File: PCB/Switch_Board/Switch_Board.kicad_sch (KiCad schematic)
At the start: 5 parts

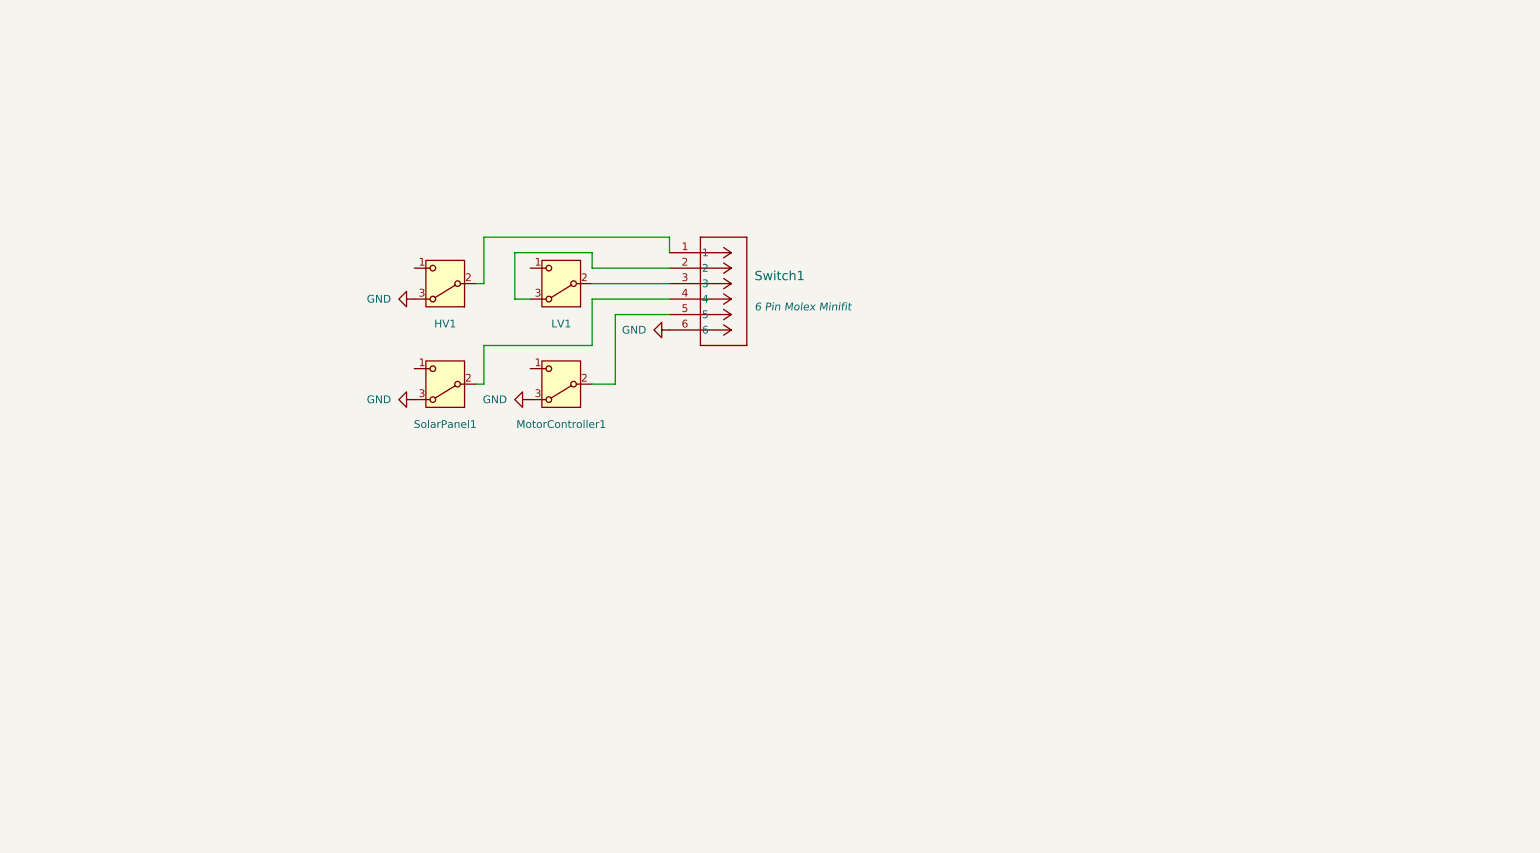
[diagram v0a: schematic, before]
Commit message: Change pinout to match BMS
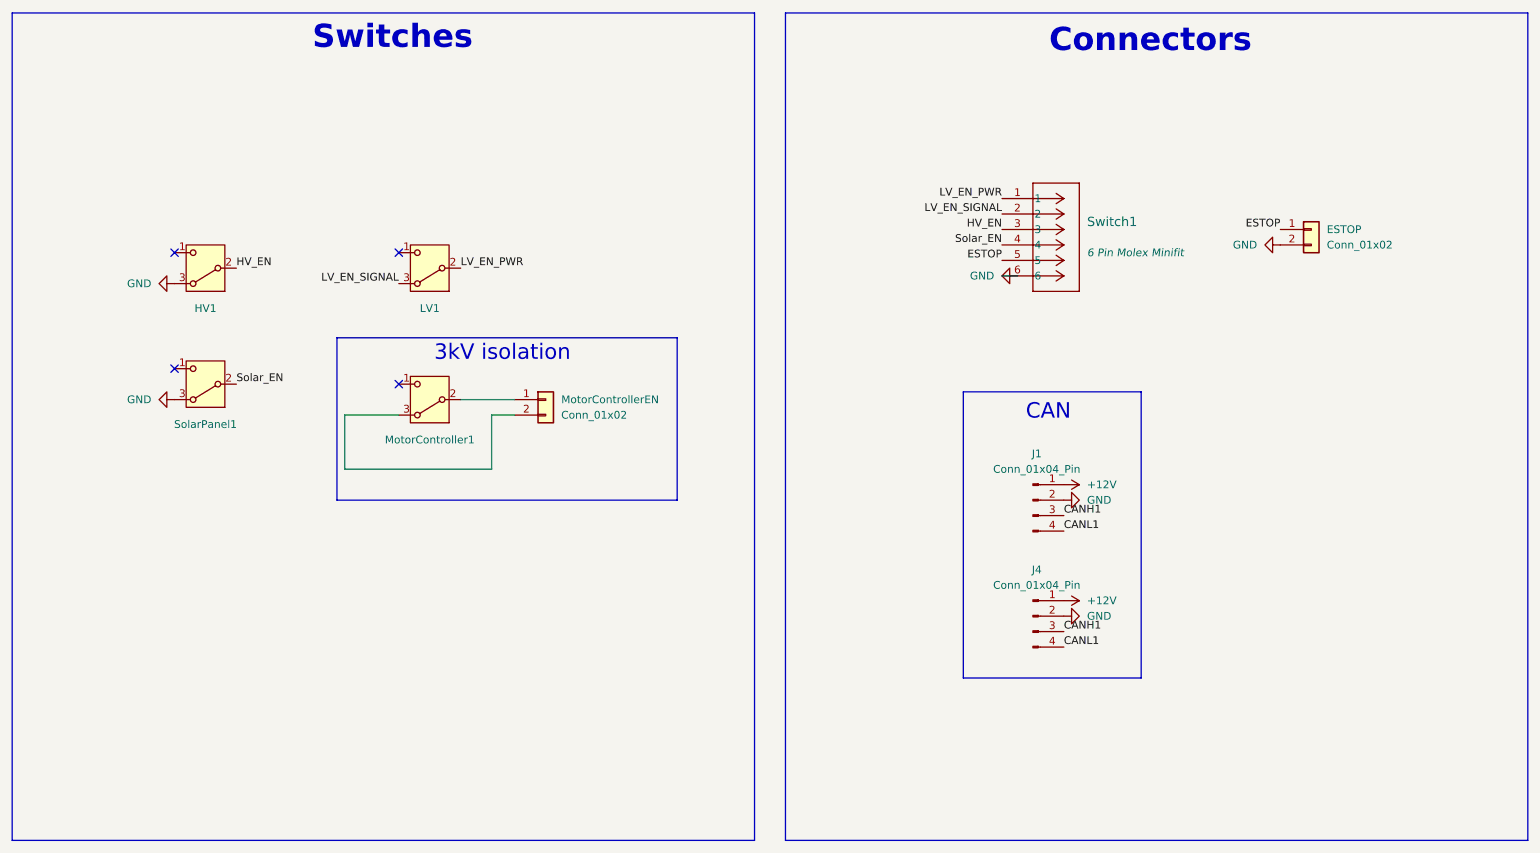
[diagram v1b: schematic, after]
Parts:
- added ESTOP, MotorControllerEN: Conn_01x02, Connector_Molex:Molex_Mini-Fit_Jr_5569-02A2_2x01_P4.20mm_Horizontal, symbol Connector_Generic:Conn_01x02
- added J1, J4: Conn_01x04_Pin, Connector_Molex:Molex_Mini-Fit_Jr_5569-04A2_2x02_P4.20mm_Horizontal, symbol Connector:Conn_01x04_Pin
- Switch1: value ~ -> (none)
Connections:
- net GND: now also ESTOP.2 (Pin_2), J1.2 (Pin_2), J4.2 (Pin_2); no longer MotorController1.3 (A)
- net Solar_EN: now reaches SolarPanel1.2 (B), Switch1.4
- net HV_EN: now reaches HV1.2 (B)
- net HV_EN: now also Switch1.3; no longer Switch1.1
- net LV_EN_PWR: now reaches LV1.2 (B)
- net LV_EN_PWR: now also Switch1.1; no longer Switch1.3
- net LV_EN_SIGNAL: now reaches LV1.3 (A), Switch1.2
- net at MotorController1.2 (B): now also MotorControllerEN.1 (Pin_1); no longer Switch1.5
- new net: MotorController1.3 (A), MotorControllerEN.2 (Pin_2)
- new net +12V: J1.1 (Pin_1), J4.1 (Pin_1)
- new net CANH1: J1.3 (Pin_3), J4.3 (Pin_3)
- new net CANL1: J1.4 (Pin_4), J4.4 (Pin_4)
- new net ESTOP: ESTOP.1 (Pin_1), Switch1.5
- no-connect marks 0 -> 4
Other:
- note added: "3kV isolation"
- note added: "CAN"
- note added: "Connectors"
- note added: "Switches"
- moved on the sheet: HV1, LV1, MotorController1, SolarPanel1, Switch1
